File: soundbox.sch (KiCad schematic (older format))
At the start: 188 parts, among them J10 COLOR INPUT, J11 MONO INPUT, J12 NEXT PWR INPUT 1, J13 NEXT PWR INPUT 2, J14 -12VDC OUT, J15 5VDC STANDBY, J16 MON IN 1, J17 MON IN 2, J18 PA1, J19 BOOT0, J2 OUT (SJ1-3535NG), J20 PC0, J21 PC1, J22 PB0, J23 PB1, J24 R SPK, J25 R SPEAKER (SJ-2509N), J26 L SPEAKER, J27 L SPK, J28 I2C Ext, J29 OLED, J3 MIC (SJ1-3535NG), J30 BOOT1, J31 NeXT Keyboard, J32 NeXT Keyboard (MD-50SM / KMDG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, J4 USB Host (SS-52100-001), J5 Mic IN, J6 Audio OUT, J7 STLINK, J8 UART2, J9 PA0, Q1 2SC2712, SW1 NeXT POWER SW (1-1825027-1 / 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, SW3 NeXT POWER SW, SW4 MCU RESET, U11 TLV70033DDCR, U17 USBLC6-2SC6, U18 STMPS2151STR‎ or TPS2051CDBV, U19 SN74LVC2G34DBV, U20 PCM5122PW, U21 TLV70033DDCR (or XC6204B332MR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, U22 TLV70033DDCR (or XC6204B332MR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, U23 PLT133/T, U24 STM32F401RCT6, U25 SN74LVC1G07DBV, U26 SN74HCT125DR, U27 TLV320ADC3100, U28 BD33FC0FP, U29 TPA2005D1DGN, U30 BD33FC0FP, U31 TPA2005D1DGN, U32 PCA9515AD, U8 5V(DC/DC), X3 ECS-2520MVLC-225.792-BN-TR, Y2 25MHz (FA-238 25.0000MB-K0)

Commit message: update value
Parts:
- U26: value SN74HCT125DR -> SN74HC125DR
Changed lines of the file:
@@
 P 5600 7050
 F 0 "U26" H 5600 7367 50  0000 C CNN
-F 1 "SN74HCT125DR" H 5600 7276 50  0000 C CNN
+F 1 "SN74HC125DR" H 5600 7276 50  0000 C CNN
 F 2 "Package_SO:SOIC-14_3.9x8.7mm_P1.27mm" H 5600 7050 50  0001 C CNN
 F 3 "http://www.ti.com/lit/gpn/sn74LS125" H 5600 7050 50  0001 C CNN
@@
 P 5800 7450
 F 0 "U26" H 5800 7767 50  0000 C CNN
-F 1 "SN74HCT125DR" H 5800 7676 50  0000 C CNN
+F 1 "SN74HC125DR" H 5800 7676 50  0000 C CNN
 F 2 "Package_SO:SOIC-14_3.9x8.7mm_P1.27mm" H 5800 7450 50  0001 C CNN
 F 3 "http://www.ti.com/lit/gpn/sn74LS125" H 5800 7450 50  0001 C CNN
@@
 P 650 6450
 F 0 "U26" H 650 6767 50  0000 C CNN
-F 1 "SN74HCT125DR" H 650 6676 50  0000 C CNN
+F 1 "SN74HC125DR" H 650 6676 50  0000 C CNN
 F 2 "Package_SO:SOIC-14_3.9x8.7mm_P1.27mm" H 650 6450 50  0001 C CNN
 F 3 "http://www.ti.com/lit/gpn/sn74LS125" H 650 6450 50  0001 C CNN
@@
 P 950 6950
 F 0 "U26" H 950 7267 50  0000 C CNN
-F 1 "SN74HCT125DR" H 950 7176 50  0000 C CNN
+F 1 "SN74HC125DR" H 950 7176 50  0000 C CNN
 F 2 "Package_SO:SOIC-14_3.9x8.7mm_P1.27mm" H 950 6950 50  0001 C CNN
 F 3 "http://www.ti.com/lit/gpn/sn74LS125" H 950 6950 50  0001 C CNN
@@
 P 1950 6900
 F 0 "U26" H 1720 6946 50  0000 R CNN
-F 1 "SN74HCT125DR" H 1720 6855 50  0000 R CNN
+F 1 "SN74HC125DR" H 1720 6855 50  0000 R CNN
 F 2 "Package_SO:SOIC-14_3.9x8.7mm_P1.27mm" H 1950 6900 50  0001 C CNN
 F 3 "http://www.ti.com/lit/gpn/sn74LS125" H 1950 6900 50  0001 C CNN

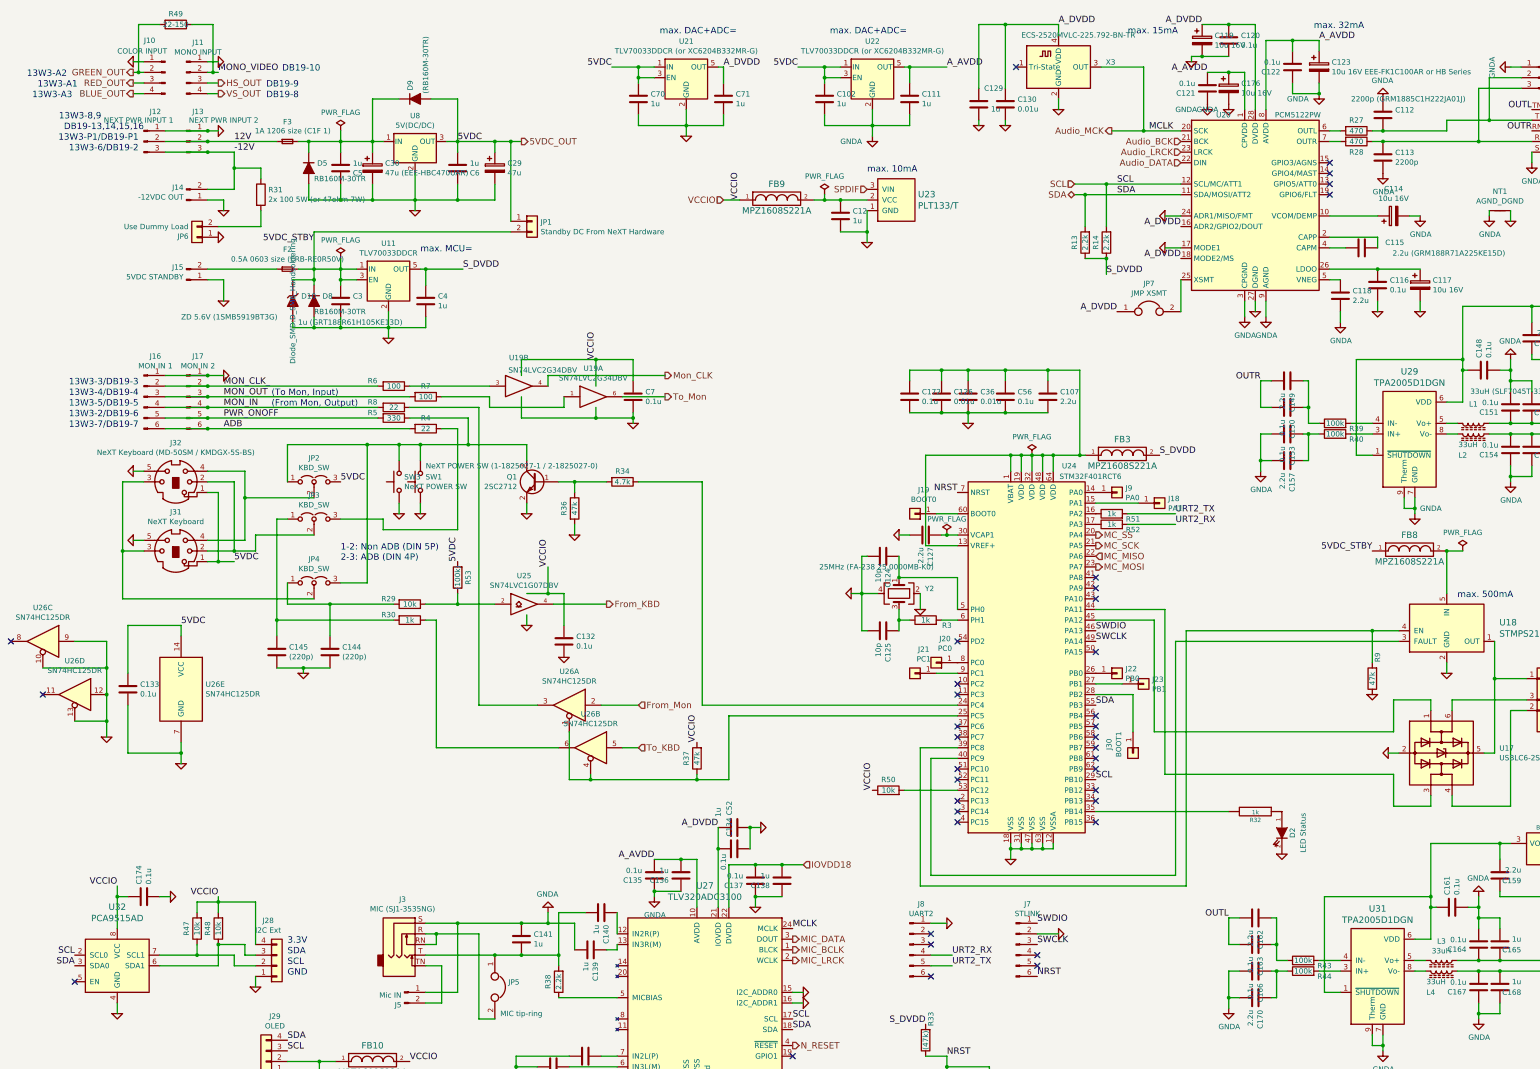
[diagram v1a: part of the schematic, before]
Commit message: move front ADB connector treat shutdown pin of the amplifier
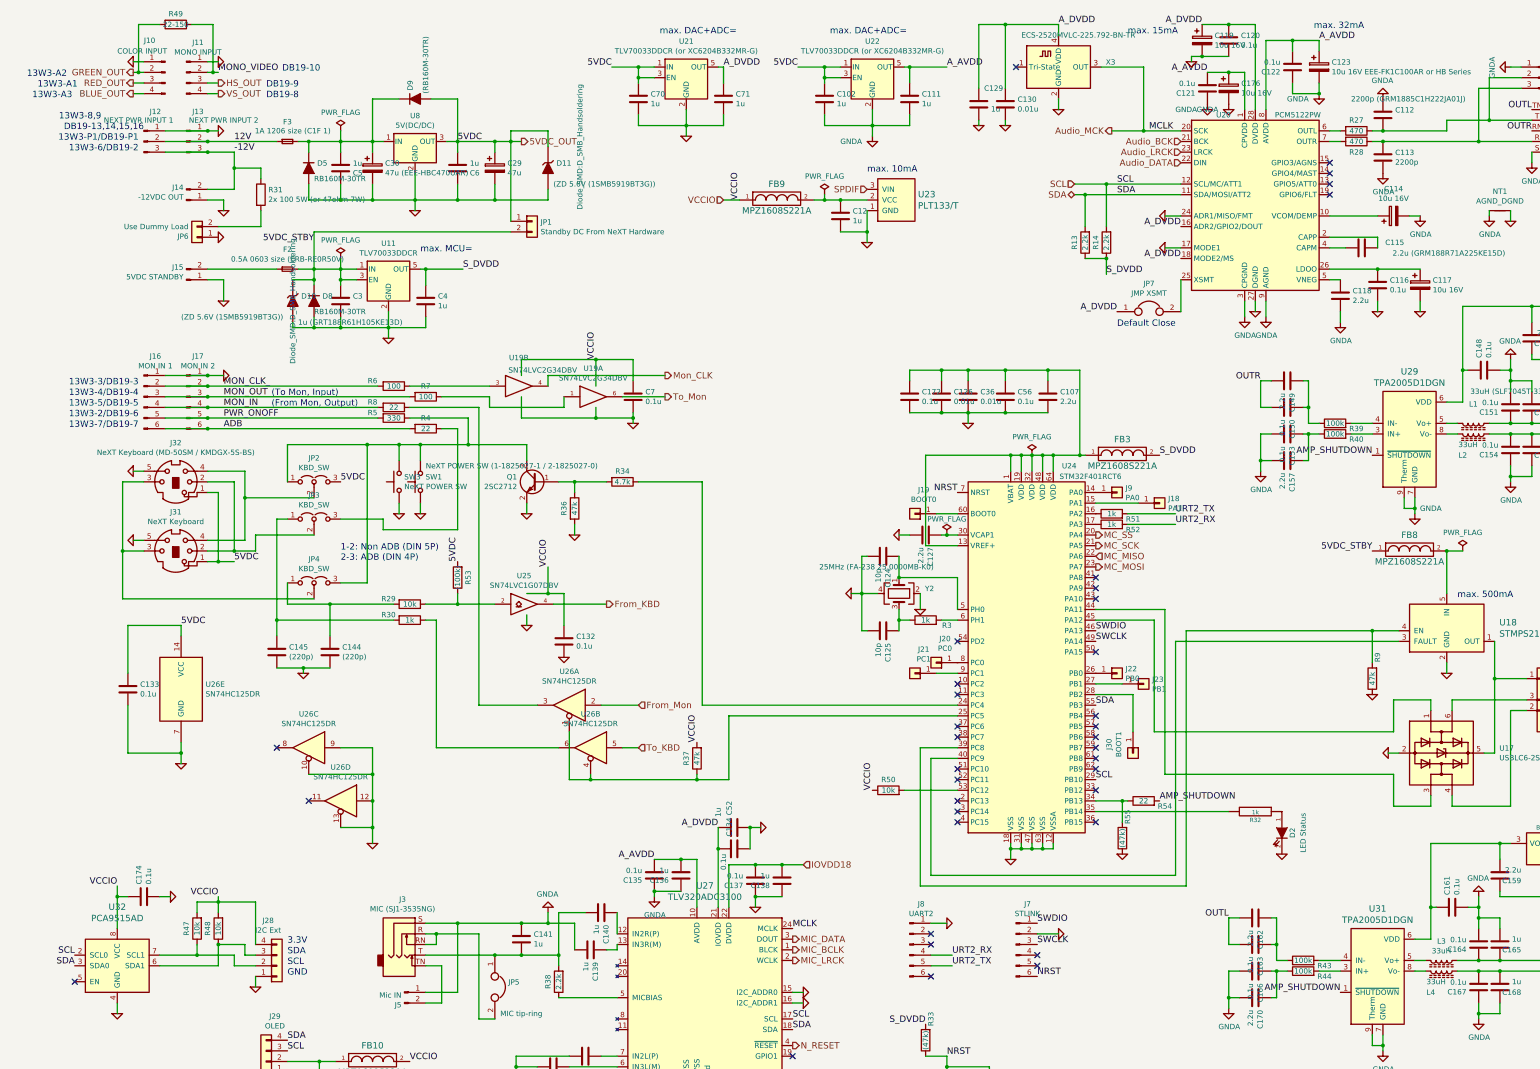
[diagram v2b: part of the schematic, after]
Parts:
- added D11: (ZD 5.6V (1SMB5919BT3G)), Diode_SMD:D_SMB_Handsoldering, symbol ossc_board-rescue:ZENER
- added R54: 22, Resistor_SMD:R_0603_1608Metric_Pad0.98x0.95mm_HandSolder, symbol Device:R
- added R55: (47k), Resistor_SMD:R_0603_1608Metric_Pad0.98x0.95mm_HandSolder, symbol Device:R
- D10: value ZD 5.6V (1SMB5919BT3G) -> (ZD 5.6V (1SMB5919BT3G))
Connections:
- net 5VDC_OUT: now also D11.1 (K)
- net GND: now also D11.2 (A), R55.1
- net at C159.2, C161.1, U30.3 (VO)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: no longer U31.1 (~SHUTDOWN)
- net at U24.34 (PB13): now also R54.1, R55.2
- net at C146.2, C148.1, U28.3 (VO)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: no longer U29.1 (~SHUTDOWN)
- new net AMP_SHUTDOWN: R54.2, U29.1 (~SHUTDOWN), U31.1 (~SHUTDOWN)
- no-connect marks 39 -> 38
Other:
- note added: "Default Close"
- moved on the sheet: U26C, U26D
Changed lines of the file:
@@
 L 74xx:74LS125 U26
 U 3 1 60B21D83
-P 650 6450
-F 0 "U26" H 650 6767 50  0000 C CNN
-F 1 "SN74HC125DR" H 650 6676 50  0000 C CNN
-F 2 "Package_SO:SOIC-14_3.9x8.7mm_P1.27mm" H 650 6450 50  0001 C CNN
-F 3 "http://www.ti.com/lit/gpn/sn74LS125" H 650 6450 50  0001 C CNN
-	3    650  6450
+P 3150 7450
+F 0 "U26" H 3150 7767 50  0000 C CNN
+F 1 "SN74HC125DR" H 3150 7676 50  0000 C CNN
+F 2 "Package_SO:SOIC-14_3.9x8.7mm_P1.27mm" H 3150 7450 50  0001 C CNN
+F 3 "http://www.ti.com/lit/gpn/sn74LS125" H 3150 7450 50  0001 C CNN
+	3    3150 7450
 	-1   0    0    -1
 $EndComp
@@
 L 74xx:74LS125 U26
 U 4 1 60B23152
-P 950 6950
-F 0 "U26" H 950 7267 50  0000 C CNN
-F 1 "SN74HC125DR" H 950 7176 50  0000 C CNN
-F 2 "Package_SO:SOIC-14_3.9x8.7mm_P1.27mm" H 950 6950 50  0001 C CNN
-F 3 "http://www.ti.com/lit/gpn/sn74LS125" H 950 6950 50  0001 C CNN
-	4    950  6950
+P 3450 7950
+F 0 "U26" H 3450 8267 50  0000 C CNN
+F 1 "SN74HC125DR" H 3450 8176 50  0000 C CNN
+F 2 "Package_SO:SOIC-14_3.9x8.7mm_P1.27mm" H 3450 7950 50  0001 C CNN
+F 3 "http://www.ti.com/lit/gpn/sn74LS125" H 3450 7950 50  0001 C CNN
+	4    3450 7950
 	-1   0    0    -1
 $EndComp
@@
 	1950 7600 1950 7500
 Connection ~ 1950 7500
-NoConn ~ 350  6450
-NoConn ~ 650  6950
+NoConn ~ 2850 7450
+NoConn ~ 3150 7950
 Text Label 1950 6300 0    60   ~ 0
 5VDC
 Wire Wire Line
-	650  6700 1250 6700
-Wire Wire Line
-	1250 6700 1250 6950
-Wire Wire Line
-	950  6450 1250 6450
-Wire Wire Line
-	1250 6450 1250 6700
-Connection ~ 1250 6700
-Wire Wire Line
-	1250 6950 1250 7200
-Wire Wire Line
-	1250 7200 950  7200
-Connection ~ 1250 6950
-Wire Wire Line
-	1250 7200 1250 7350
-Connection ~ 1250 7200
+	3150 7700 3750 7700
+Wire Wire Line
+	3750 7700 3750 7950
+Wire Wire Line
+	3450 7450 3750 7450
+Wire Wire Line
+	3750 7450 3750 7700
+Connection ~ 3750 7700
+Wire Wire Line
+	3750 7950 3750 8200
+Wire Wire Line
+	3750 8200 3450 8200
+Connection ~ 3750 7950
+Wire Wire Line
+	3750 8200 3750 8350
+Connection ~ 3750 8200
 $Comp
 L ossc_board-rescue:GND-RESCUE-ossc_board #PWR091
 U 1 1 60CD63A4
-P 1250 7350
-F 0 "#PWR091" H 1250 7350 30  0001 C CNN
-F 1 "GND-RESCUE-ossc_board" H 1250 7280 30  0001 C CNN
-F 2 "" H 1250 7350 60  0000 C CNN
-F 3 "" H 1250 7350 60  0000 C CNN
-	1    1250 7350
+P 3750 8350
+F 0 "#PWR091" H 3750 8350 30  0001 C CNN
+F 1 "GND-RESCUE-ossc_board" H 3750 8280 30  0001 C CNN
+F 2 "" H 3750 8350 60  0000 C CNN
+F 3 "" H 3750 8350 60  0000 C CNN
+	1    3750 8350
 	1    0    0    -1
 $EndComp
@@
 NoConn ~ 10550 7650
 NoConn ~ 10550 7850
-NoConn ~ 10550 7950
 NoConn ~ 10550 8150
 NoConn ~ 9250 8150
@@
 Wire Wire Line
 	13550 9250 13700 9250
-Wire Wire Line
-	12850 9750 12700 9750
-Wire Wire Line
-	12700 9750 12700 8850
-Wire Wire Line
-	12700 8850 13700 8850
-Wire Wire Line
-	13700 8850 13700 8950
 $Comp
 L Device:R R43
@@
 Wire Wire Line
 	14350 8350 13700 8350
-Wire Wire Line
-	13700 8350 13700 8850
 Connection ~ 14350 8350
-Connection ~ 13700 8850
 Wire Wire Line
 	14350 8800 14350 8850
@@
 Wire Wire Line
 	13850 4200 14000 4200
-Wire Wire Line
-	13150 4700 13000 4700
-Wire Wire Line
-	13000 4700 13000 3800
-Wire Wire Line
-	13000 3800 14000 3800
-Wire Wire Line
-	14000 3800 14000 3900
 $Comp
 L Device:R R39
@@
 Wire Wire Line
 	14650 3300 14000 3300
-Wire Wire Line
-	14000 3300 14000 3800
 Connection ~ 14650 3300
-Connection ~ 14000 3800
 Wire Wire Line
 	14650 3750 14650 3800
@@
 P 3000 3250
 F 0 "D10" V 2954 3329 50  0000 L CNN
-F 1 "ZD 5.6V (1SMB5919BT3G)" V 3150 2200 50  0000 L CNN
+F 1 "(ZD 5.6V (1SMB5919BT3G))" V 3150 2200 50  0000 L CNN
 F 2 "Diode_SMD:D_SMB_Handsoldering" H 3000 3250 50  0000 C CNN
 F 3 "" H 3000 3250 50  0000 C CNN
@@
 Wire Wire Line
 	5500 9000 5500 9400
+Text Notes 10750 3500 0    60   ~ 0
+Default Close
+Wire Wire Line
+	14000 3300 14000 3900
+Text Label 13150 4700 2    60   ~ 0
+AMP_SHUTDOWN
+Wire Wire Line
+	13700 8350 13700 8950
+Text Label 12850 9750 2    60   ~ 0
+AMP_SHUTDOWN
+Text Label 11150 7950 0    60   ~ 0
+AMP_SHUTDOWN
+$Comp
+L Device:R R55
+U 1 1 6100A350
+P 10800 8300
+F 0 "R55" V 10750 8100 50  0000 C CNN
+F 1 "(47k)" V 10800 8300 50  0000 C CNN
+F 2 "Resistor_SMD:R_0603_1608Metric_Pad0.98x0.95mm_HandSolder" V 10730 8300 50  0001 C CNN
+F 3 "~" H 10800 8300 50  0001 C CNN
+	1    10800 8300
+	-1   0    0    1
+$EndComp
+$Comp
+L Device:R R54
+U 1 1 6100BDEC
+P 11000 7950
+F 0 "R54" V 10950 7750 50  0000 C CNN
+F 1 "22" V 11000 7950 50  0000 C CNN
+F 2 "Resistor_SMD:R_0603_1608Metric_Pad0.98x0.95mm_HandSolder" V 10930 7950 50  0001 C CNN
+F 3 "~" H 11000 7950 50  0001 C CNN
+	1    11000 7950
+	0    -1   -1   0
+$EndComp
+Wire Wire Line
+	10550 7950 10800 7950
+Wire Wire Line
+	10800 7950 10800 8150
+Connection ~ 10800 7950
+Wire Wire Line
+	10800 7950 10850 7950
+$Comp
+L ossc_board-rescue:GND-RESCUE-ossc_board #PWR0273
+U 1 1 610F77EE
+P 10800 8450
+F 0 "#PWR0273" H 10800 8450 30  0001 C CNN
+F 1 "GND-RESCUE-ossc_board" H 10800 8380 30  0001 C CNN
+F 2 "" H 10800 8450 60  0000 C CNN
+F 3 "" H 10800 8450 60  0000 C CNN
+	1    10800 8450
+	1    0    0    -1
+$EndComp
+$Comp
+L ossc_board-rescue:ZENER D11
+U 1 1 611333D2
+P 5400 2000
+F 0 "D11" V 5354 2079 50  0000 L CNN
+F 1 "(ZD 5.6V (1SMB5919BT3G))" V 5550 2050 50  0000 L CNN
+F 2 "Diode_SMD:D_SMB_Handsoldering" H 5200 2300 50  0000 C CNN
+F 3 "" H 5400 2000 50  0000 C CNN
+	1    5400 2000
+	0    1    1    0
+$EndComp
+Wire Wire Line
+	5400 2200 5400 2300
+Wire Wire Line
+	5400 2300 4900 2300
+Connection ~ 4900 2300
+Wire Wire Line
+	5400 1800 5400 1650
+Wire Wire Line
+	5400 1650 5050 1650
+Wire Wire Line
+	5050 1650 5050 1750
 $EndSCHEMATC

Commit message: minor update
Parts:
- C174, C175: value 0.1u -> (0.1u)
- FB10: value MPZ1608S221A -> (MPZ1608S221A)
- R47, R48: value 10k -> (10k)
- U32: value PCA9515AD -> (PCA9515AD)
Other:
- note added: "This block is optional."
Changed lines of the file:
@@
 Text Label 3450 4950 0    60   ~ 0
 5VDC
-Text Notes 3450 5700 0    60   ~ 0
+Text Notes 3300 5700 0    60   ~ 0
 1-2: Non ADB (DIN 5P)\n2-3: ADB (DIN 4P)
 Wire Wire Line
@@
 P 1350 9750
 F 0 "U32" H 1350 10553 60  0000 C CNN
-F 1 "PCA9515AD" H 1350 10447 60  0000 C CNN
+F 1 "(PCA9515AD)" H 1350 10447 60  0000 C CNN
 F 2 "Package_SO:SOIC-8_3.9x4.9mm_P1.27mm" H 1350 9750 60  0001 C CNN
 F 3 "" H 1350 9750 60  0001 C CNN
@@
 P 1600 8850
 F 0 "C174" H 1715 8896 50  0000 L CNN
-F 1 "0.1u" H 1715 8805 50  0000 L CNN
+F 1 "(0.1u)" H 1715 8805 50  0000 L CNN
 F 2 "Capacitor_SMD:C_0603_1608Metric_Pad1.05x0.95mm_HandSolder" H 1638 8700 50  0001 C CNN
 F 3 "~" H 1600 8850 50  0001 C CNN
@@
 P 2100 9150
 F 0 "R47" V 2200 9150 50  0000 C CNN
-F 1 "10k" V 2100 9150 50  0000 C CNN
+F 1 "(10k)" V 2100 9150 50  0000 C CNN
 F 2 "Resistor_SMD:R_0603_1608Metric_Pad1.05x0.95mm_HandSolder" V 2030 9150 50  0001 C CNN
 F 3 "~" H 2100 9150 50  0001 C CNN
@@
 P 2300 9150
 F 0 "R48" V 2400 9150 50  0000 C CNN
-F 1 "10k" V 2300 9150 50  0000 C CNN
+F 1 "(10k)" V 2300 9150 50  0000 C CNN
 F 2 "Resistor_SMD:R_0603_1608Metric_Pad1.05x0.95mm_HandSolder" V 2230 9150 50  0001 C CNN
 F 3 "~" H 2300 9150 50  0001 C CNN
@@
 AR Path="/5F595115/5FC89A27" Ref="FB10"  Part="1"
 F 0 "FB10" H 3750 10550 60  0000 C CNN
-F 1 "MPZ1608S221A" H 3750 10300 60  0000 C CNN
+F 1 "(MPZ1608S221A)" H 3750 10300 60  0000 C CNN
 F 2 "Inductor_SMD:L_0603_1608Metric_Pad1.05x0.95mm_HandSolder" H 3750 10400 60  0001 C CNN
 F 3 "~" H 3750 10400 60  0000 C CNN
@@
 P 3250 10650
 F 0 "C175" H 3365 10696 50  0000 L CNN
-F 1 "0.1u" H 3365 10605 50  0000 L CNN
+F 1 "(0.1u)" H 3365 10605 50  0000 L CNN
 F 2 "Capacitor_SMD:C_0603_1608Metric_Pad1.05x0.95mm_HandSolder" H 3288 10500 50  0001 C CNN
 F 3 "~" H 3250 10650 50  0001 C CNN
@@
 Wire Wire Line
 	5050 1650 5050 1750
+Text Notes 950  10100 0    60   ~ 0
+This block is optional.
+Text Notes 2700 11050 0    60   ~ 0
+This block is optional.
 $EndSCHEMATC

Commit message: value update
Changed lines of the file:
@@
 P 3200 3250
 F 0 "D8" V 3154 3329 50  0000 L CNN
-F 1 "RB160M-30TR" V 3300 3250 50  0000 L CNN
+F 1 "RB160M-30TR" V 3550 3000 50  0000 L CNN
 F 2 "custom_components:D_SOD-123_HandSoldering" H 3200 3250 50  0001 C CNN
 F 3 "~" H 3200 3250 50  0001 C CNN
@@
 P 3450 3250
 F 0 "C3" H 3565 3296 50  0000 L CNN
-F 1 "1u (GRT188R61H105KE13D)" H 3050 3050 50  0000 L CNN
+F 1 "1u (GRT188R61H105KE13D)" H 3400 3050 50  0000 L CNN
 F 2 "Capacitor_SMD:C_0603_1608Metric_Pad1.05x0.95mm_HandSolder" H 3488 3100 50  0001 C CNN
 F 3 "~" H 3450 3250 50  0001 C CNN
@@
 F 0 "D10" V 2954 3329 50  0000 L CNN
 F 1 "(ZD 5.6V (1SMB5919BT3G))" V 3150 2200 50  0000 L CNN
-F 2 "Diode_SMD:D_SMB_Handsoldering" H 3000 3250 50  0000 C CNN
+F 2 "Diode_SMD:D_SMB_Handsoldering" V 3250 2600 50  0001 C CNN
 F 3 "" H 3000 3250 50  0000 C CNN
 	1    3000 3250
@@
 F 0 "D11" V 5354 2079 50  0000 L CNN
 F 1 "(ZD 5.6V (1SMB5919BT3G))" V 5550 2050 50  0000 L CNN
-F 2 "Diode_SMD:D_SMB_Handsoldering" H 5200 2300 50  0000 C CNN
+F 2 "Diode_SMD:D_SMB_Handsoldering" H 5200 2300 50  0001 C CNN
 F 3 "" H 5400 2000 50  0000 C CNN
 	1    5400 2000

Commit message: add comment
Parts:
- R31: value 2x 100 5W (or 47ohm 7W) -> 100//100 5W (or 47ohm 7W)
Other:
- note added: "-12V Dummy Load for older PSU"
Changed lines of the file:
@@
 P 2700 2250
 F 0 "R31" H 2770 2296 50  0000 L CNN
-F 1 "2x 100 5W (or 47ohm 7W)" H 2770 2205 50  0000 L CNN
+F 1 "100//100 5W (or 47ohm 7W)" H 2770 2205 50  0000 L CNN
 F 2 "Resistor_THT:R_Axial_DIN0617_L17.0mm_D6.0mm_P30.48mm_Horizontal" V 2630 2250 50  0001 C CNN
 F 3 "~" H 2700 2250 50  0001 C CNN
@@
 Text Notes 2700 11050 0    60   ~ 0
 This block is optional.
+Text Notes 2750 2500 0    60   ~ 0
+-12V Dummy Load for older PSU
 $EndSCHEMATC
